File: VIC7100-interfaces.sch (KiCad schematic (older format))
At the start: 76 parts, among them Q5 BSS138AKA, U13 VIC7100

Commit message: Update naming convention
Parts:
- C173, C174, C175, C183, C185, C186, C187, C189, C198, C199, C202: footprint arv-som-footprints:0402-cap -> arvsom-footprints:0402-cap; symbol arv-som:C_1u_0402 -> arvsom:C_1u_0402
- C176, C177, C178, C179, C180, C181, C188, C190, C191, C192, C193, C194, C195, C196, C197, C200, C201, C203, C204, C205, C206: footprint arv-som-footprints:0201-res -> arvsom-footprints:0201-res; symbol arv-som:C_100n_0201 -> arvsom:C_100n_0201
- C182, C184: footprint arv-som-footprints:0402-cap -> arvsom-footprints:0402-cap; symbol arv-som:C_10u_0402 -> arvsom:C_10u_0402
- D4: footprint arv-som-footprints:LED_0603 -> arvsom-footprints:LED_0603; symbol arv-som:KP-1608CGCK -> arvsom:KP-1608CGCK
- FB6: footprint arv-som-footprints:0402-res -> arvsom-footprints:0402-res; symbol arv-som:BLM15PD121SN1D -> arvsom:BLM15PD121SN1D
- Q5: footprint arv-som-footprints:SOT-23-3 -> arvsom-footprints:SOT-23-3; symbol arv-som:BSS138AKA -> arvsom:BSS138AKA
- R117, R118: footprint arv-som-footprints:0402-res -> arvsom-footprints:0402-res; symbol arv-som:R_2k_0402 -> arvsom:R_2k_0402
- R119, R55, R56, R57, R58, R59: footprint arv-som-footprints:0402-res -> arvsom-footprints:0402-res; symbol arv-som:R_33R_0402 -> arvsom:R_33R_0402
- R120: footprint arv-som-footprints:0402-res -> arvsom-footprints:0402-res; symbol arv-som:R_1k_0402 -> arvsom:R_1k_0402
- R122: footprint arv-som-footprints:0402-res -> arvsom-footprints:0402-res; symbol arv-som:R_10k_0402 -> arvsom:R_10k_0402
- R60, R61, R62, R63, R64, R65, R66, R67, R68, R69, R70, R71, R72, R73, R74, R75, R76, R77, R78, R79, R80, R81, R82, R83, R84, R85, R86, R87: footprint arv-som-footprints:0201-res -> arvsom-footprints:0201-res; symbol arv-som:R_33R_0201 -> arvsom:R_33R_0201
- U13: footprint arv-som-footprints:vic7100 -> arvsom-footprints:vic7100; symbol arv-som:VIC7100 -> arvsom:VIC7100

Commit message: Updated GPIO pinout to BV0.9. Remapped DSI. Mapped USB3.0
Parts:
- removed R117, R118: R_2k_0402, arvsom-footprints:0402-res, symbol arvsom:R_2k_0402
- added R117, R118, R? (x2): R_4k7_0402, arvsom-footprints:0402-res, symbol arvsom:R_4k7_0402
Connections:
- net labels added: CDTX_DSI_CK_N, CDTX_DSI_CK_P, GP43_LED, GPIO0, GPIO1, GPIO10, GPIO11, GPIO12, GPIO13, GPIO14, GPIO15, GPIO16, GPIO17, GPIO18, GPIO19, GPIO2, GPIO20, GPIO21, GPIO22, GPIO23, GPIO24, GPIO3, GPIO4, GPIO44, GPIO45, GPIO46, GPIO47, GPIO48, GPIO5, GPIO55_GMAC_RESETN, GPIO6, GPIO63_GMAC_RESETN, GPIO7, GPIO8, GPIO9, RES_SSRX2_N, RES_SSRX2_P, RES_SSTX2_N, RES_SSTX2_P, USB_SSRX1_N, USB_SSRX1_P, USB_SSTX1N, USB_SSTX1P
- net labels removed: CDTX_DSI_D2_N, CDTX_DSI_D2_P, CDTX_DSI_D3_N, CDTX_DSI_D3_P, CDTX_DSI_D4_N, CDTX_DSI_D4_P, LED, PWR_OFF, RPI_GPIO10, RPI_GPIO11, RPI_GPIO12, RPI_GPIO13, RPI_GPIO14, RPI_GPIO15, RPI_GPIO16, RPI_GPIO17, RPI_GPIO18, RPI_GPIO19, RPI_GPIO2, RPI_GPIO20, RPI_GPIO21, RPI_GPIO22, RPI_GPIO23, RPI_GPIO24, RPI_GPIO25, RPI_GPIO26, RPI_GPIO27, RPI_GPIO3, RPI_GPIO4, RPI_GPIO5, RPI_GPIO6, RPI_GPIO7, RPI_GPIO8, RPI_GPIO9, RPI_ID_SC, RPI_ID_SD, SDIO0_CD
- wire segments 263 -> 273
- no-connect marks 59 -> 49
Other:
- note added: "Not mapped on B2B"
- note added: "Reserved\n"
- note removed: "TBD: put PCIe interface here"
- note removed: "TODO:\nadd on/off logic connection\nto PWR_OFF pin"
- note removed: "USB_SSRXA1"
- note removed: "USB_SSRXA2"
- note removed: "USB_SSRXB1"
- note removed: "USB_SSRXB2"
- note removed: "USB_SSTXA1"
- note removed: "USB_SSTXA2"
- note removed: "USB_SSTXB1"
- note removed: "USB_SSTXB2"
- note removed: "X2C_TX_CLK"
- note removed: "X2C_TX_RST"
- note removed: "X2C_TX_SEND"
- moved on the sheet: R122, R55, R56, R57, R58, R59

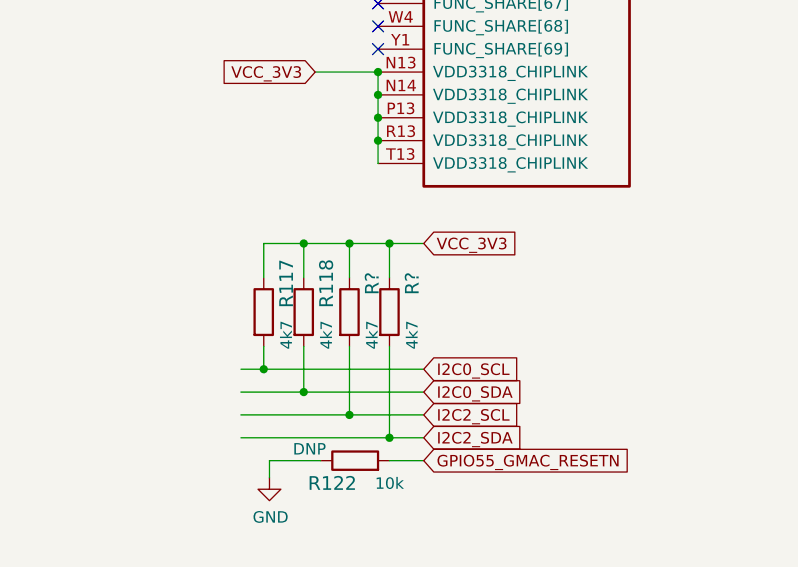
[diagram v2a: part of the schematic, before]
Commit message: Updated VIC config, added reset and crystals
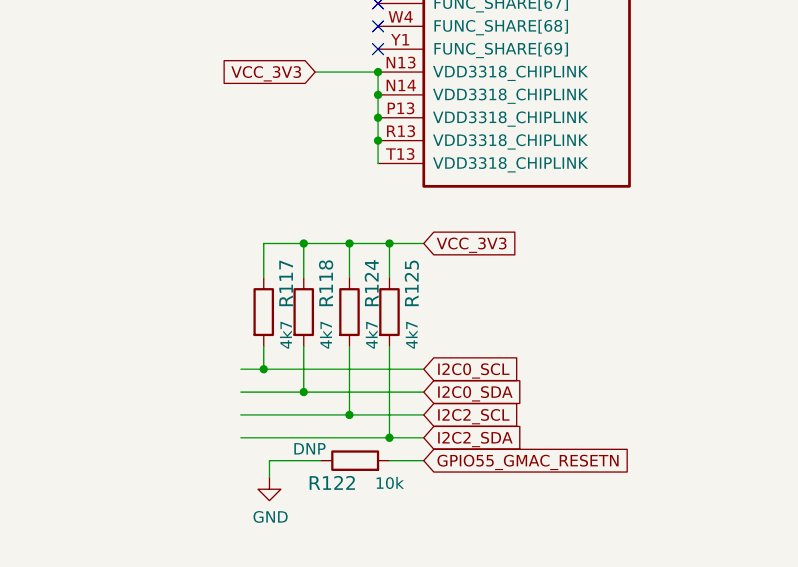
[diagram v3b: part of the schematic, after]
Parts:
- gave numbers to parts that had none: 2
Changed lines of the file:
@@
 $EndComp
 $Comp
-L arvsom:R_4k7_0402 R?
+L arvsom:R_4k7_0402 R124
 U 1 1 610B85F4
 P 2000 9325
-F 0 "R?" H 1875 9425 60  0000 C CNN
+F 0 "R124" H 1875 9425 60  0000 C CNN
 F 1 "R_4k7_0402" H 2000 9175 60  0001 C CNN
 F 2 "arvsom-footprints:0402-res" H 2200 9525 60  0001 L CNN
@@
 $EndComp
 $Comp
-L arvsom:R_4k7_0402 R?
+L arvsom:R_4k7_0402 R125
 U 1 1 610B88A9
 P 2175 9325
-F 0 "R?" H 2050 9425 60  0000 C CNN
+F 0 "R125" H 2050 9425 60  0000 C CNN
 F 1 "R_4k7_0402" H 2175 9175 60  0001 C CNN
 F 2 "arvsom-footprints:0402-res" H 2375 9525 60  0001 L CNN

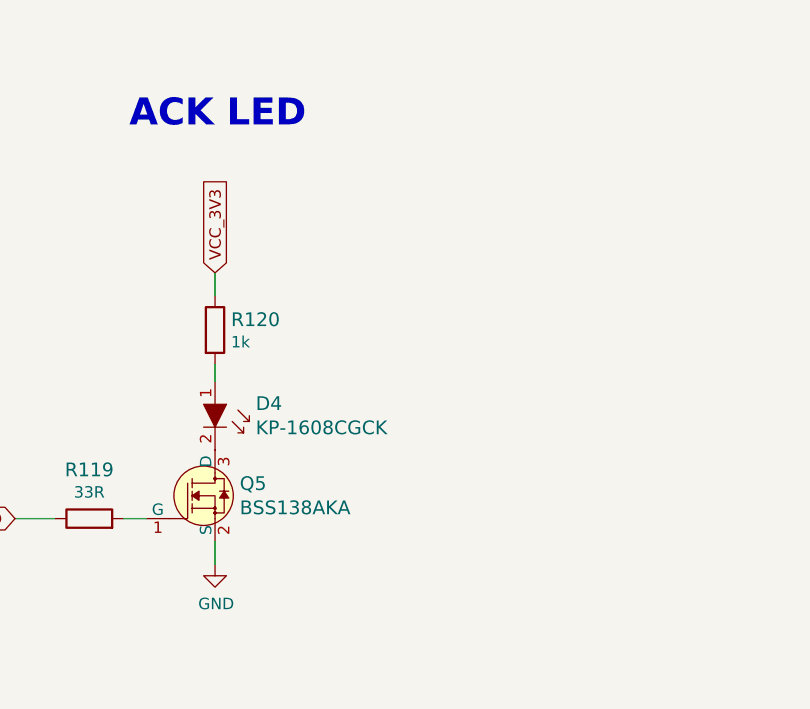
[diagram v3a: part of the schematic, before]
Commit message: Added BOOT_FROM_UART and power LED. Changed LED transistor to smaller footprint
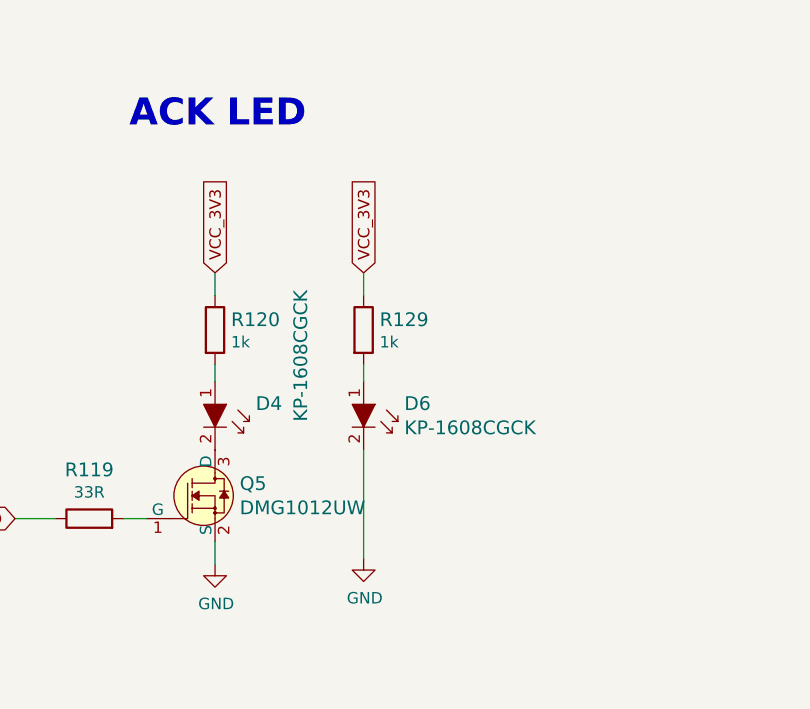
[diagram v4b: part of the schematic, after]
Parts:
- removed Q5: BSS138AKA, arvsom-footprints:SOT-23-3, symbol arvsom:BSS138AKA
- added D6: KP-1608CGCK, arvsom-footprints:LED_0603, symbol arvsom:KP-1608CGCK
- added Q5: DMG1012UW, arvsom-footprints:SOT-323, symbol arvsom:DMG1012UW
- added R129: R_1k_0402, arvsom-footprints:0402-res, symbol arvsom:R_1k_0402
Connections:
- net GND: now also D6.2, Q5.2 (S)
- net VCC_3V3: now also R129.1
- net at D4.2: now also Q5.3 (D)
- net at R119.2: now also Q5.1 (G)
- new net: D6.1, R129.2
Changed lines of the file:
@@
 P 9200 9350
 F 0 "D4" V 9097 9528 60  0000 L CNN
-F 1 "KP-1608CGCK" V 9203 9528 60  0000 L CNN
+F 1 "KP-1608CGCK" H 8600 9725 60  0000 L CNN
 F 2 "arvsom-footprints:LED_0603" H 9400 9550 60  0001 L CNN
 F 3 "http://www.farnell.com/datasheets/2045956.pdf" H 9400 9650 60  0001 L CNN
@@
 Wire Wire Line
 	9200 8675 9200 8775
-$Comp
-L arvsom:BSS138AKA Q5
-U 1 1 631064ED
-P 9200 9650
-F 0 "Q5" H 9308 9703 60  0000 L CNN
-F 1 "BSS138AKA" H 9308 9597 60  0000 L CNN
-F 2 "arvsom-footprints:SOT-23-3" H 9400 9850 60  0001 L CNN
-F 3 "https://www.onsemi.com/pub/Collateral/BSS138-D.PDF" H 9400 9950 60  0001 L CNN
-F 4 "BSS138AKAR" H 9400 10150 60  0001 L CNN "MPN"
-F 5 "ON Semiconductor" H 9400 10750 60  0001 L CNN "Manufacturer"
-	1    9200 9650
-	1    0    0    -1
-$EndComp
 Wire Wire Line
 	9200 9850 9200 9950
@@
 Text Notes 8025 5600 0    50   ~ 0
 Reserved\n
+$Comp
+L arvsom:DMG1012UW Q5
+U 1 1 60A4B638
+P 9200 9650
+F 0 "Q5" H 9308 9703 60  0000 L CNN
+F 1 "DMG1012UW" H 9308 9597 60  0000 L CNN
+F 2 "arvsom-footprints:SOT-323" H 9400 9850 60  0001 L CNN
+F 3 "http://www.farnell.com/datasheets/2814383.pdf" H 9400 9950 60  0001 L CNN
+F 4 "DMG1012UW" H 9400 10150 60  0001 L CNN "MPN"
+F 5 "Diodes Incorporated" H 9400 10750 60  0001 L CNN "Manufacturer"
+	1    9200 9650
+	1    0    0    -1
+$EndComp
+$Comp
+L arvsom:R_1k_0402 R129
+U 1 1 60B1C76B
+P 9850 8925
+F 0 "R129" V 9805 8995 60  0000 L CNN
+F 1 "R_1k_0402" H 9850 8775 60  0001 C CNN
+F 2 "arvsom-footprints:0402-res" H 10050 9125 60  0001 L CNN
+F 3 "" H 9850 8925 50  0001 C CNN
+F 4 "BOURNS" H 10050 9325 60  0001 L CNN "Manufacturer"
+F 5 "CR0402-FX-1001GLF" H 10050 9225 60  0001 L CNN "MPN"
+F 6 "1k" V 9903 8995 50  0000 L CNN "Val"
+	1    9850 8925
+	0    1    1    0
+$EndComp
+$Comp
+L arvsom:KP-1608CGCK D6
+U 1 1 60B1C773
+P 9850 9350
+F 0 "D6" V 9747 9528 60  0000 L CNN
+F 1 "KP-1608CGCK" V 9853 9528 60  0000 L CNN
+F 2 "arvsom-footprints:LED_0603" H 10050 9550 60  0001 L CNN
+F 3 "http://www.farnell.com/datasheets/2045956.pdf" H 10050 9650 60  0001 L CNN
+F 4 "KP-1608CGCK" H 10050 9850 60  0001 L CNN "MPN"
+F 5 "KINGBRIGHT" H 10060 9970 60  0001 L CNN "Manufacturer"
+	1    9850 9350
+	0    1    1    0
+$EndComp
+Wire Wire Line
+	9850 9075 9850 9150
+Text GLabel 9850 8675 1    50   Input ~ 0
+VCC_3V3
+Wire Wire Line
+	9850 8675 9850 8775
+$Comp
+L arvsom:GND #PWR?
+U 1 1 60B32959
+P 9850 9925
+AR Path="/607683D6/60B32959" Ref="#PWR?"  Part="1"
+AR Path="/60805CEC/60B32959" Ref="#PWR014"  Part="1"
+F 0 "#PWR014" H 9850 9675 50  0001 C CNN
+F 1 "GND" H 9855 9752 50  0000 C CNN
+F 2 "" H 9850 9925 50  0001 C CNN
+F 3 "" H 9850 9925 50  0001 C CNN
+	1    9850 9925
+	1    0    0    -1
+$EndComp
+Wire Wire Line
+	9850 9925 9850 9450
 $EndSCHEMATC

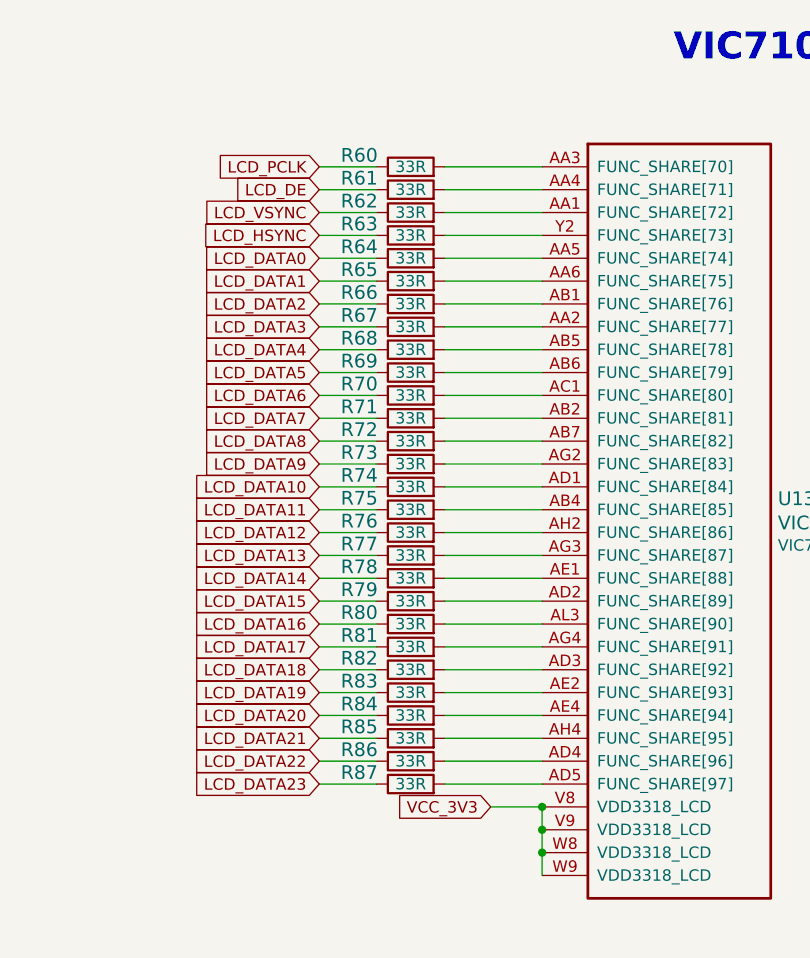
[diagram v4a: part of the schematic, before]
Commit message: Replaced 33R groups with resistor arrays
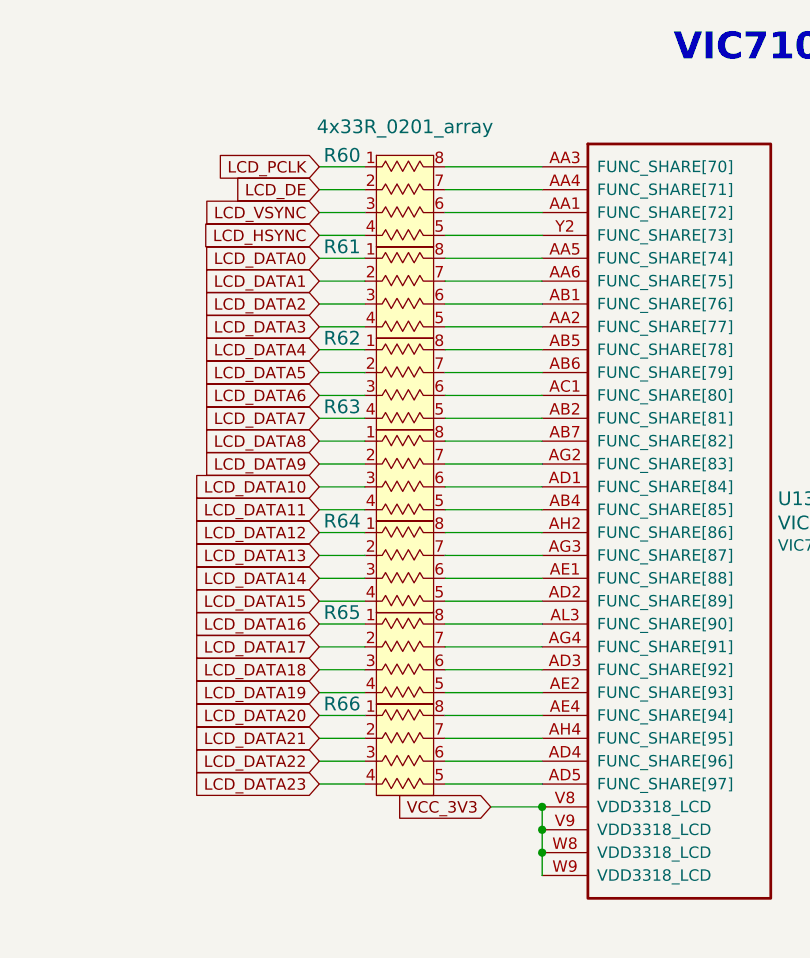
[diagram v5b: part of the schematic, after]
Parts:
- removed R60, R61, R62, R63, R64, R65, R66, R67, R68, R69, R70, R71, R72, R73, R74, R75, R76, R77, R78, R79, R80, R81, R82, R83, R84, R85, R86, R87: R_33R_0201, arvsom-footprints:0201-res, symbol arvsom:R_33R_0201
- added R60, R61, R62, R63, R64, R65, R66: 4x33R_0201_array, arvsom-footprints:EXB18V, symbol arvsom:4x33R_0201_array
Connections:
- net LCD_DATA0: now also R61.1
- net LCD_DATA1: now also R61.2
- net LCD_DATA10: now also R63.3
- net LCD_DATA11: now also R63.4
- net LCD_DATA12: now also R64.1
- net LCD_DATA13: now also R64.2
- net LCD_DATA14: now also R64.3
- net LCD_DATA15: now also R64.4
- net LCD_DATA16: now also R65.1
- net LCD_DATA17: now also R65.2
- net LCD_DATA18: now also R65.3
- net LCD_DATA19: now also R65.4
- net LCD_DATA2: now also R61.3
- net LCD_DATA20: now also R66.1
- net LCD_DATA21: now also R66.2
- net LCD_DATA22: now also R66.3
- net LCD_DATA23: now also R66.4
- net LCD_DATA3: now also R61.4
- net LCD_DATA4: now also R62.1
- net LCD_DATA5: now also R62.2
- net LCD_DATA6: now also R62.3
- net LCD_DATA7: now also R62.4
- net LCD_DATA8: now also R63.1
- net LCD_DATA9: now also R63.2
- net LCD_DE: now also R60.2
- net LCD_HSYNC: now also R60.4
- net LCD_PCLK: now also R60.1
- net LCD_VSYNC: now also R60.3
- net at U13.AA1 (FUNC_SHARE[72]): now also R60.6
- net at U13.AA2 (FUNC_SHARE[77]): now also R61.5
- net at U13.AA3 (FUNC_SHARE[70]): now also R60.8
- net at U13.AA4 (FUNC_SHARE[71]): now also R60.7
- net at U13.AA5 (FUNC_SHARE[74]): now also R61.8
- net at U13.AA6 (FUNC_SHARE[75]): now also R61.7
- net at U13.AB1 (FUNC_SHARE[76]): now also R61.6
- net at U13.AB2 (FUNC_SHARE[81]): now also R62.5
- net at U13.AB4 (FUNC_SHARE[85]): now also R63.5
- net at U13.AB5 (FUNC_SHARE[78]): now also R62.8
- net at U13.AB6 (FUNC_SHARE[79]): now also R62.7
- net at U13.AB7 (FUNC_SHARE[82]): now also R63.8
- net at U13.AC1 (FUNC_SHARE[80]): now also R62.6
- net at U13.AD1 (FUNC_SHARE[84]): now also R63.6
- net at U13.AD2 (FUNC_SHARE[89]): now also R64.5
- net at U13.AD3 (FUNC_SHARE[92]): now also R65.6
- net at U13.AD4 (FUNC_SHARE[96]): now also R66.6
- net at U13.AD5 (FUNC_SHARE[97]): now also R66.5
- net at U13.AE1 (FUNC_SHARE[88]): now also R64.6
- net at U13.AE2 (FUNC_SHARE[93]): now also R65.5
- net at U13.AE4 (FUNC_SHARE[94]): now also R66.8
- net at U13.AG2 (FUNC_SHARE[83]): now also R63.7
- net at U13.AG3 (FUNC_SHARE[87]): now also R64.7
- net at U13.AG4 (FUNC_SHARE[91]): now also R65.7
- net at U13.AH2 (FUNC_SHARE[86]): now also R64.8
- net at U13.AH4 (FUNC_SHARE[95]): now also R66.7
- net at U13.AL3 (FUNC_SHARE[90]): now also R65.8
- net at U13.Y2 (FUNC_SHARE[73]): now also R60.5

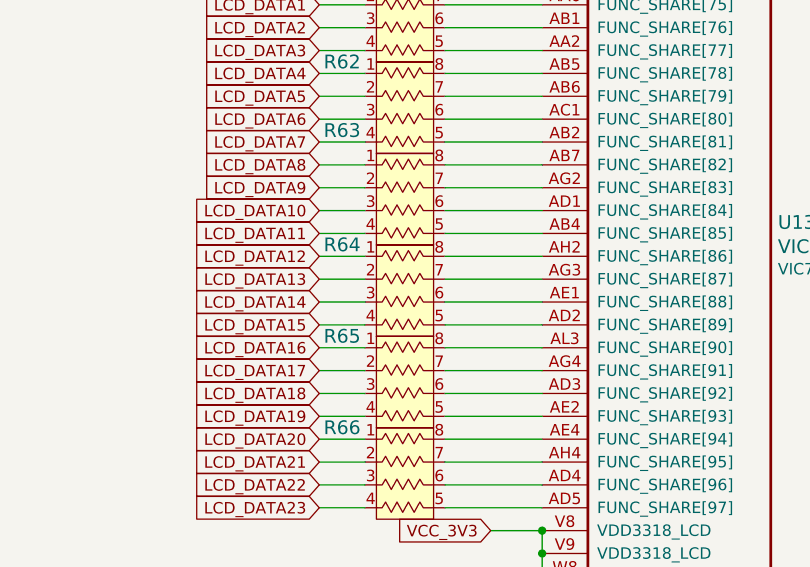
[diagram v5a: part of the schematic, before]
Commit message: Updated component placement - HDMI IC passives, QSPI, 5V8 buck placed
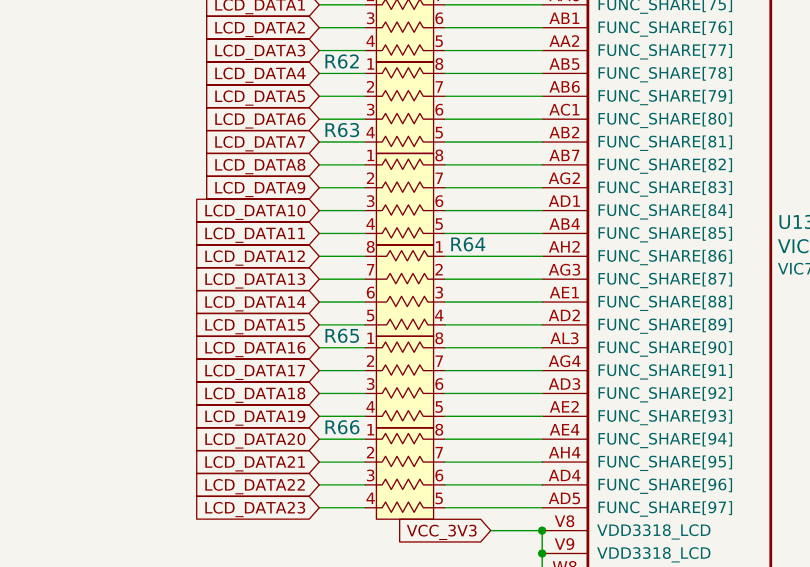
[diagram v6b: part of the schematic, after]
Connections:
- net LCD_DATA12: now also R64.8; no longer R64.1
- net LCD_DATA13: now also R64.7; no longer R64.2
- net LCD_DATA14: now also R64.6; no longer R64.3
- net LCD_DATA15: now also R64.5; no longer R64.4
- net at U13.AD2 (FUNC_SHARE[89]): now also R64.4; no longer R64.5
- net at U13.AE1 (FUNC_SHARE[88]): now also R64.3; no longer R64.6
- net at U13.AG3 (FUNC_SHARE[87]): now also R64.2; no longer R64.7
- net at U13.AH2 (FUNC_SHARE[86]): now also R64.1; no longer R64.8
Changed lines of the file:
@@
 L arvsom:4x33R_0201_array R64
 U 1 1 60A9EF05
-P 5125 3300
-F 0 "R64" H 4825 3750 60  0000 C CNN
-F 1 "4x33R_0201_array" H 5100 3881 60  0001 C CNN
-F 2 "arvsom-footprints:EXB18V" H 4925 4050 60  0001 L CNN
-F 3 "http://industrial.panasonic.com/cdbs/www-data/pdf/AOC0000/AOC0000C14.pdf" H 4925 4050 60  0001 L CNN
-F 4 "EXB-18V330JX" H 4925 4250 60  0001 L CNN "MPN"
-F 5 "Panasonic" H 4925 4150 60  0001 L CNN "Manufacturer"
-	1    5125 3300
-	1    0    0    -1
+P 5075 3300
+F 0 "R64" H 4775 3750 60  0000 C CNN
+F 1 "4x33R_0201_array" H 5050 3881 60  0001 C CNN
+F 2 "arvsom-footprints:EXB18V" H 4875 4050 60  0001 L CNN
+F 3 "http://industrial.panasonic.com/cdbs/www-data/pdf/AOC0000/AOC0000C14.pdf" H 4875 4050 60  0001 L CNN
+F 4 "EXB-18V330JX" H 4875 4250 60  0001 L CNN "MPN"
+F 5 "Panasonic" H 4875 4150 60  0001 L CNN "Manufacturer"
+	1    5075 3300
+	-1   0    0    -1
 $EndComp
 $Comp
